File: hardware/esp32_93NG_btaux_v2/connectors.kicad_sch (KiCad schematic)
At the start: 6 parts, among them J2 I2S_MIC, J3 PROG, J4 Conn_01x02_Male, J5 Conn_01x02_Male, J6 Conn_01x02_Male, J7 Conn_01x02_Male

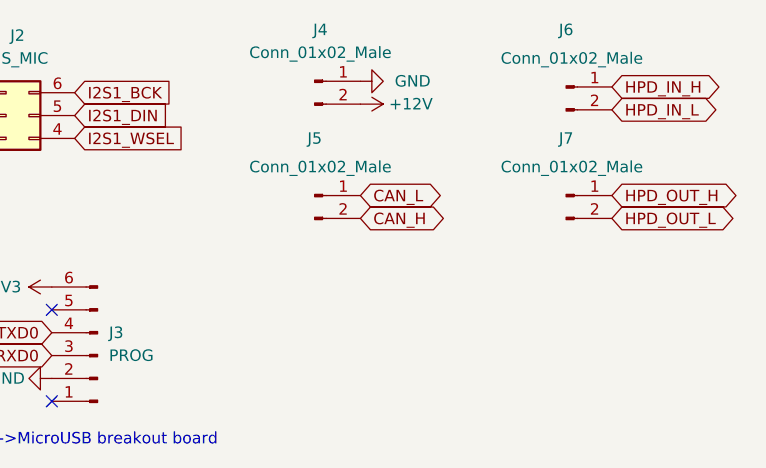
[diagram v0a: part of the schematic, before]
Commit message: Added top and bottom faceplates. Improved silkscreen labels for pinouts, buttons, connectors.
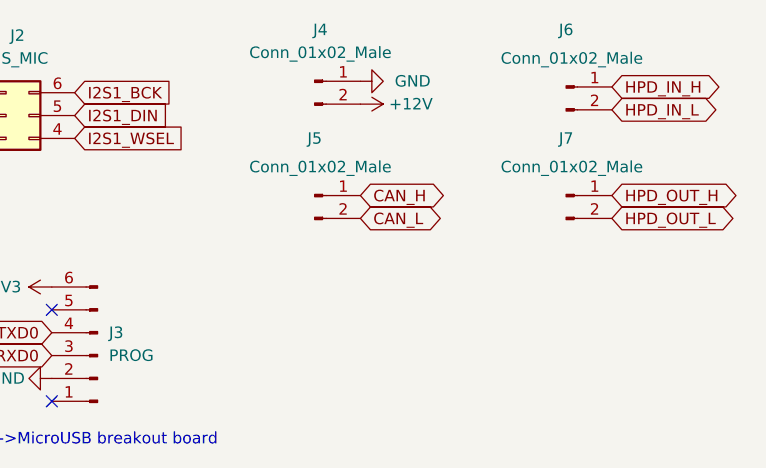
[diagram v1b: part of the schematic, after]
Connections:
- net CAN_H: now also J5.1 (Pin_1); no longer J5.2 (Pin_2)
- net CAN_L: now also J5.2 (Pin_2); no longer J5.1 (Pin_1)
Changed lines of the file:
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@@
     (effects (font (size 1.27 1.27)) (justify left bottom))
-  )
-  (global_label "CAN_H" (shape bidirectional) (at 129.54 91.44 0) (fields_autoplaced)
-    (effects (font (size 1.27 1.27)) (justify left))
-    (property "Intersheet References" "${INTERSHEET_REFS}" (id 0) (at 137.9402 91.5194 0)
-      (effects (font (size 1.27 1.27)) (justify left) hide)
-    )
   )
   (global_label "I2S1_BCK" (shape input) (at 97.79 77.47 0) (fields_autoplaced)
@@
     )
   )
+  (global_label "CAN_L" (shape bidirectional) (at 129.54 91.44 0) (fields_autoplaced)
+    (effects (font (size 1.27 1.27)) (justify left))
+    (property "Intersheet References" "${INTERSHEET_REFS}" (id 0) (at 137.6379 91.3606 0)
+      (effects (font (size 1.27 1.27)) (justify left) hide)
+    )
+  )
   (global_label "HPD_OUT_H" (shape bidirectional) (at 157.48 88.9 0) (fields_autoplaced)
     (effects (font (size 1.27 1.27)) (justify left))
@@
     )
   )
-  (global_label "CAN_L" (shape bidirectional) (at 129.54 88.9 0) (fields_autoplaced)
+  (global_label "CAN_H" (shape bidirectional) (at 129.54 88.9 0) (fields_autoplaced)
     (effects (font (size 1.27 1.27)) (justify left))
-    (property "Intersheet References" "${INTERSHEET_REFS}" (id 0) (at 137.6379 88.9794 0)
+    (property "Intersheet References" "${INTERSHEET_REFS}" (id 0) (at 137.9402 88.8206 0)
       (effects (font (size 1.27 1.27)) (justify left) hide)
     )

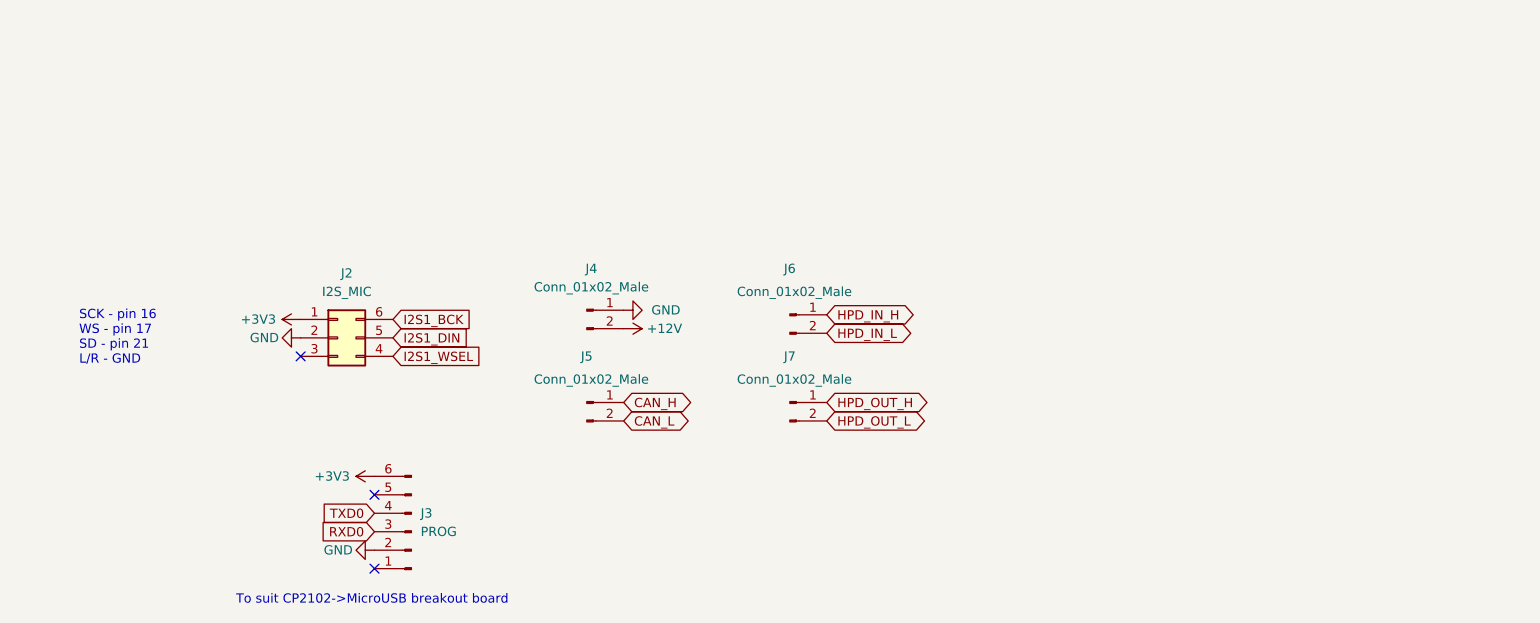
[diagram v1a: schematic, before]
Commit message: Adjusted silkscreen labels to reduce clutter. Added GPIO header for external buttons or LEDs. Added second PCB faceplate, for the bottom-side of the assembly.
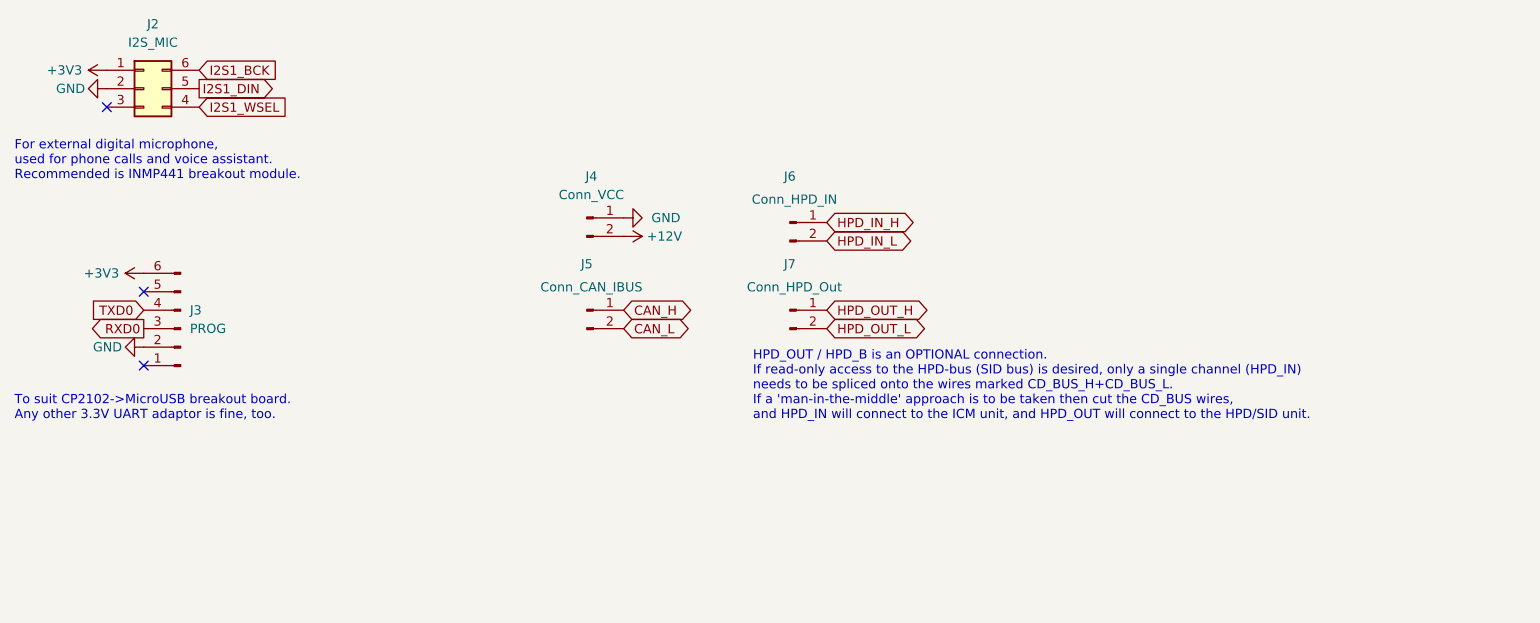
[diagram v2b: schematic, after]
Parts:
- J4: value Conn_01x02_Male -> Conn_VCC
- J5: value Conn_01x02_Male -> Conn_CAN_IBUS
- J6: value Conn_01x02_Male -> Conn_HPD_IN
- J7: value Conn_01x02_Male -> Conn_HPD_Out
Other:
- note added: "For external digital microphone, used for phone calls and voice assistant. Recommended is INMP441 breakout module."
- note added: "HPD_OUT / HPD_B is an OPTIONAL connection. If read-only access to the HPD-bus (SID bus) is desired, only a single channel (HPD_IN) needs to be spliced onto the wires marked CD_BUS_H+CD_BUS_L. If a 'man-in-the-middle' approach is to be taken then cut the CD_BUS wires, and HPD_IN will connect to the ICM unit, and HPD_OUT will connect to the HPD/SID unit."
- note added: "To suit CP2102->MicroUSB breakout board. Any other 3.3V UART adaptor is fine, too."
- note removed: "SCK - pin 16 WS - pin 17 SD - pin 21 L/R - GND"
- note removed: "To suit CP2102->MicroUSB breakout board"
- moved on the sheet: J2, J3, J4, J5, J6, J7
